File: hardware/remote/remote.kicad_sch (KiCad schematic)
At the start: 34 parts, among them J1 USB-C, Q1 MMBT3904, Q2 MMBT3904, SW1 UP, SW2 DOWN, SW3 ON/OFF, U1 TP4056, U2 ME6211C33M5G, U3 ESP32-WROOM-32, U4 CP2102

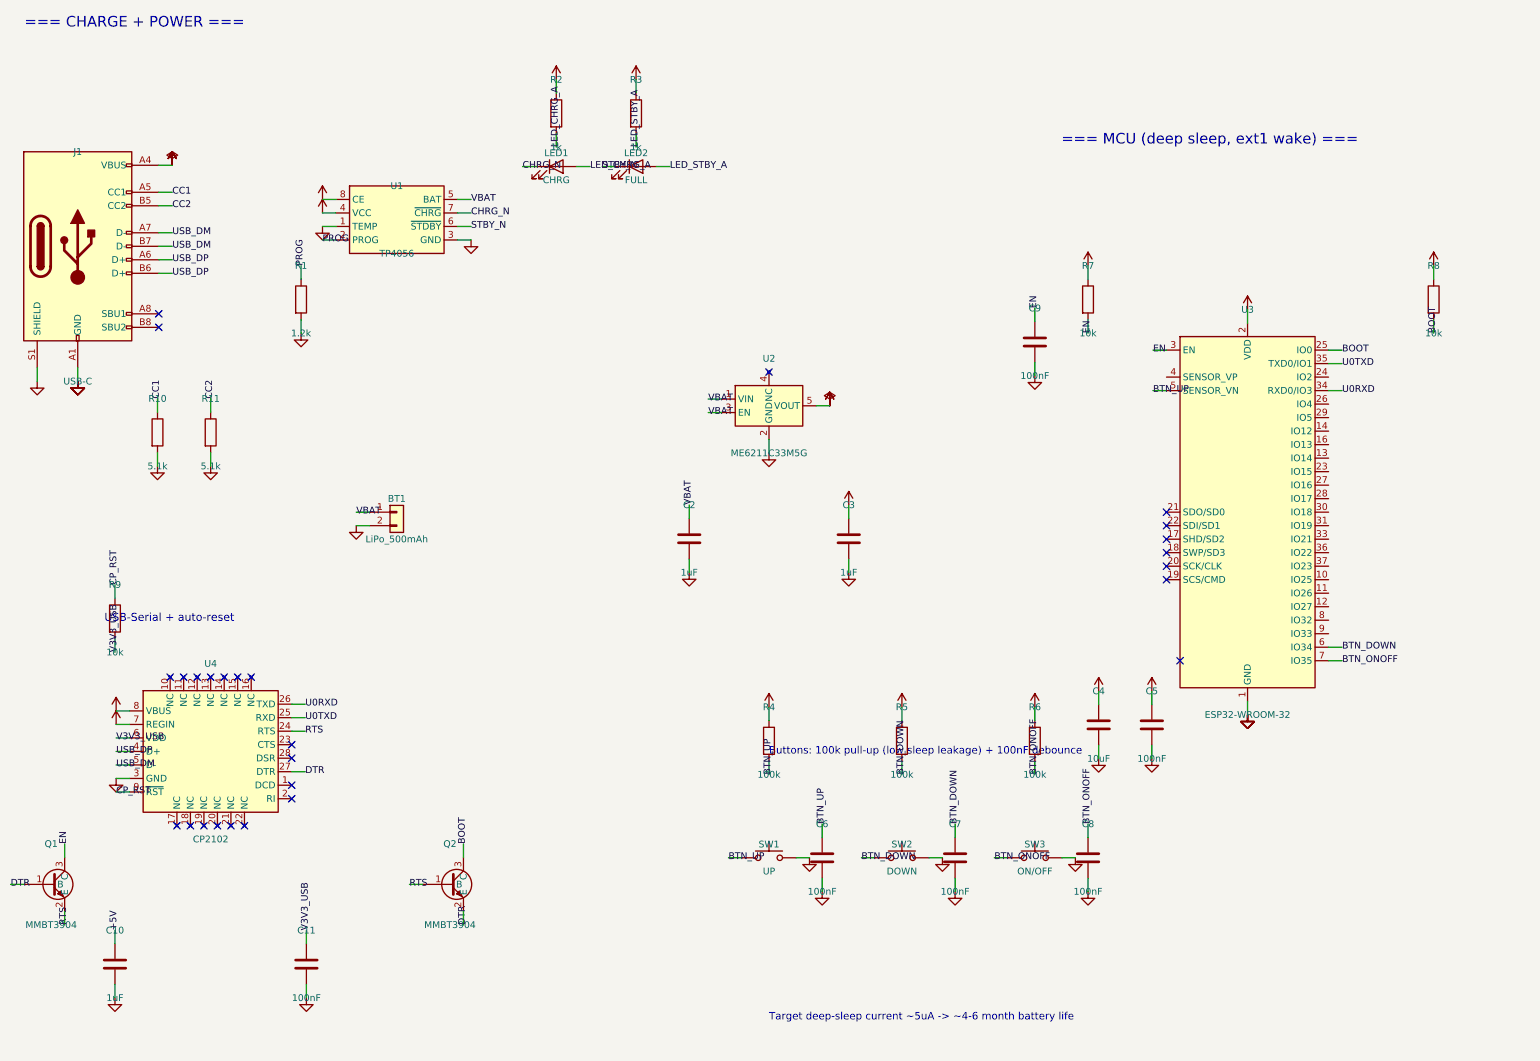
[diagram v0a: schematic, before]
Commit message: hardware: switch both boards to plug-in modules (ESP32 DevKit, TP4056)
Rework the schematic capture so every part maps to a hand-solderable module
or component you can buy from Robu / Robocraze / Quartz Components, per the
"hand-solder from modules" plan.

Both boards:
- Replace the bare ESP32-WROOM-32 + the entire onboard USB-serial subsystem
  (CP2102 QFN, board USB-C + CC resistors, two-transistor auto-reset, CP2102
  support caps/pull-ups, separate BOOT/EN buttons) with a plug-in ESP32
  DevKit V1 (30-pin) that carries its own USB bridge, micro-USB, auto-reset
  and BOOT/EN. Carrier now only routes 3V3/GND + the GPIOs it uses.

Remote:
- TP4056 bare SOP-8 -> TP4056 charge+protect module (charges via its own
  USB-C); external charge LEDs + PROG resistor removed (onboard the module).
  B+/B- -> LiPo, OUT+/OUT- -> ME6211 input.
- Tactile buttons -> 6mm THT footprint (SW_PUSH_6mm).
- Note: DevKit leaks in deep sleep, so battery life drops from months to
  days/weeks (accepted trade for simplicity; documented in CLAUDE.md).

parts.py: add ESP32_DevKit() and TP4056_module() symbols; drop bare CP2102 /
TP4056. Regenerated via gen_dimmer.py / gen_remote.py; validate.py reports no
floating pins on either board. Schematic files normalize back to the
generator's 20230121 format (KiCad 10 re-upgrades on open).
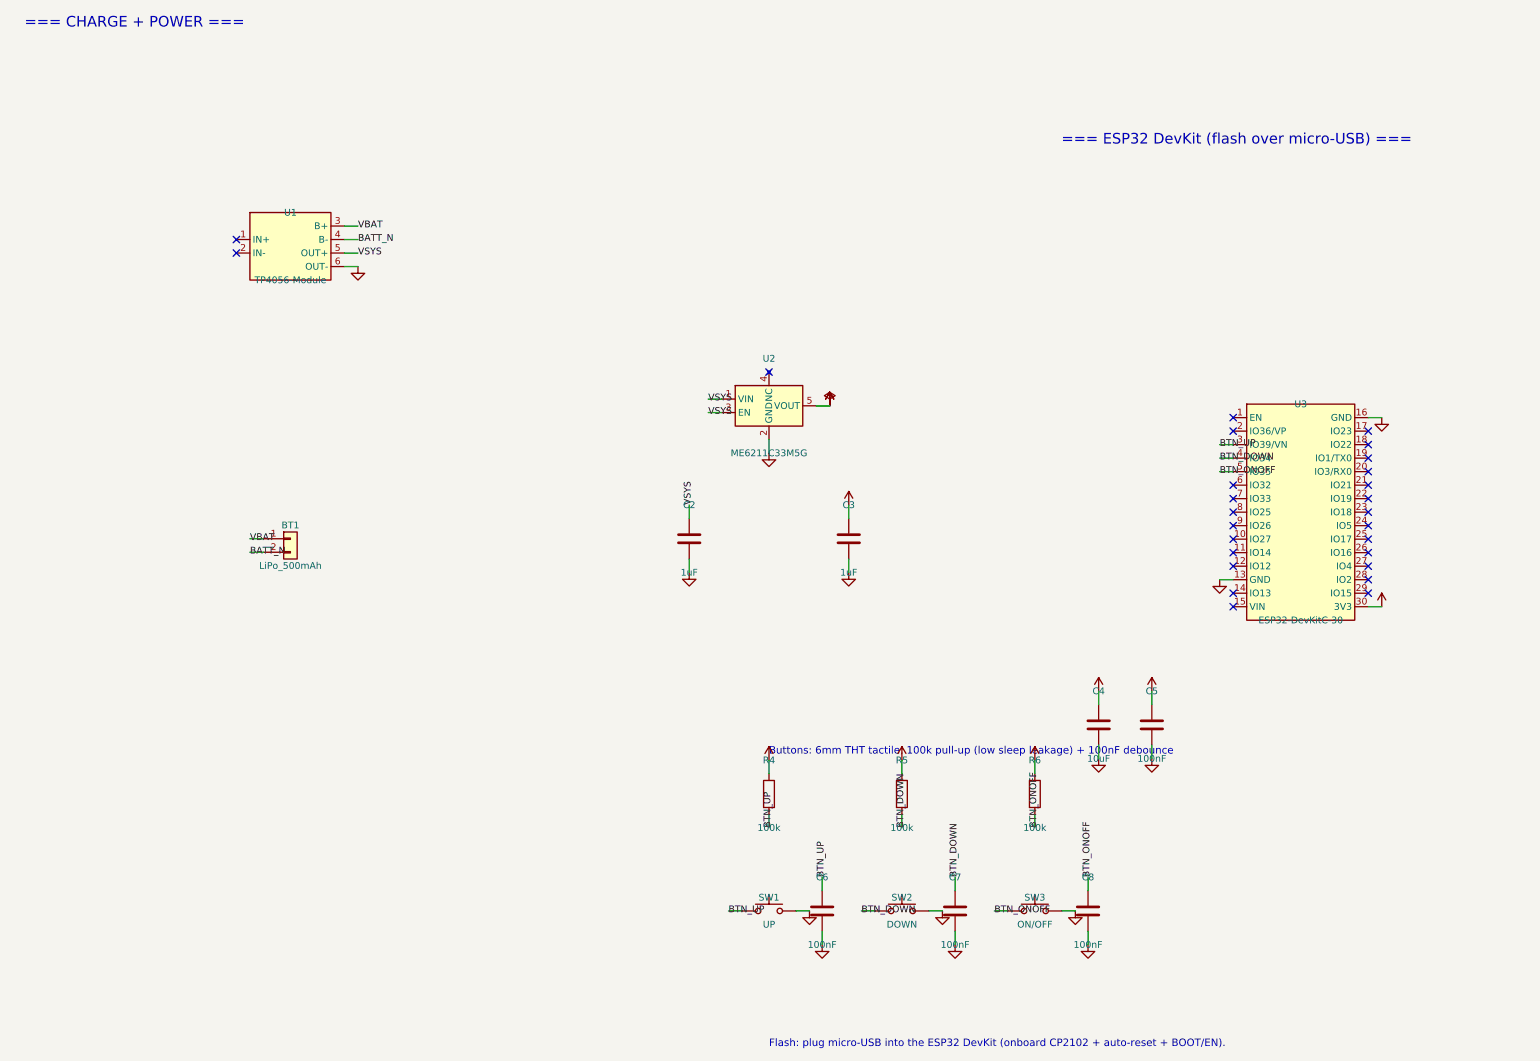
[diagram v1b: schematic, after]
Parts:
- removed C10: 1uF, Capacitor_SMD:C_0805_2012Metric, symbol Device:C
- removed C11, C9: 100nF, Capacitor_SMD:C_0805_2012Metric, symbol Device:C
- removed J1: USB-C, Connector_USB:USB_C_Receptacle_HRO_TYPE-C-31-M-12, symbol Connector:USB_C_Receptacle_USB2.0_16P
- removed LED1: CHRG, LED_SMD:LED_0805_2012Metric, symbol Device:LED
- removed LED2: FULL, LED_SMD:LED_0805_2012Metric, symbol Device:LED
- removed Q1, Q2: MMBT3904, Package_TO_SOT_SMD:SOT-23, symbol Transistor_BJT:MMBT3904
- removed R1: 1.2k, Resistor_SMD:R_0805_2012Metric, symbol Device:R
- removed R10, R11: 5.1k, Resistor_SMD:R_0805_2012Metric, symbol Device:R
- removed R2, R3: 1k, Resistor_SMD:R_0805_2012Metric, symbol Device:R
- removed R7, R8, R9: 10k, Resistor_SMD:R_0805_2012Metric, symbol Device:R
- removed U1: TP4056, Package_SO:SOIC-8_3.9x4.9mm_P1.27mm, symbol Battery_Management:TP4056
- removed U3: ESP32-WROOM-32, RF_Module:ESP32-WROOM-32, symbol RF_Module:ESP32-WROOM-32
- removed U4: CP2102, Package_DFN_QFN:QFN-28-1EP_5x5mm_P0.5mm, symbol Interface_USB:CP2102
- added U1: TP4056-Module, Connector_PinHeader_2.54mm:PinHeader_1x06_P2.54mm_Vertical, symbol Battery_Management:TP4056_Module
- added U3: ESP32-DevKitC-30, Module:ESP32-DevKitC, symbol Module:ESP32-DevKitC
- SW1, SW2, SW3: footprint Button_Switch_SMD:SW_SPST_PTS645 -> Button_Switch_THT:SW_PUSH_6mm
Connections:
- net +3V3: now also U3.30 (3V3)
- net BTN_DOWN: now also U3.4 (IO34)
- net BTN_ONOFF: now also U3.5 (IO35)
- net BTN_UP: now also U3.3 (IO39/VN)
- net GND: now also U1.6 (OUT-), U3.13 (GND), U3.16 (GND); no longer BT1.2 (Pin_2)
- net VBAT: now also U1.3 (B+); no longer C2.1, U2.1 (VIN), U2.3 (EN)
- new net BATT_N: BT1.2 (Pin_2), U1.4 (B-)
- new net VSYS: C2.1, U1.5 (OUT+), U2.1 (VIN), U2.3 (EN)
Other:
- note added: "=== ESP32 DevKit (flash over micro-USB) ==="
- note added: "Buttons: 6mm THT tactile, 100k pull-up (low sleep leakage) + 100nF debounce"
- note added: "Flash: plug micro-USB into the ESP32 DevKit (onboard CP2102 + auto-reset + BOOT/EN)."
- note removed: "=== MCU (deep sleep, ext1 wake) ==="
- note removed: "Buttons: 100k pull-up (low sleep leakage) + 100nF debounce"
- note removed: "Target deep-sleep current ~5uA -> ~4-6 month battery life"
- note removed: "USB-Serial + auto-reset"

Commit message: hardware: annotate both schematics with block boxes, headers, net legend
Add color-coded functional-block rectangles, colored block-title text,
and a signal/net-legend glossary to the dimmer and remote schematics for
readability. Also upgrades both .kicad_sch to KiCad 10 format. Netlist
connectivity verified unchanged on both boards (dimmer 12 nets, remote 8).
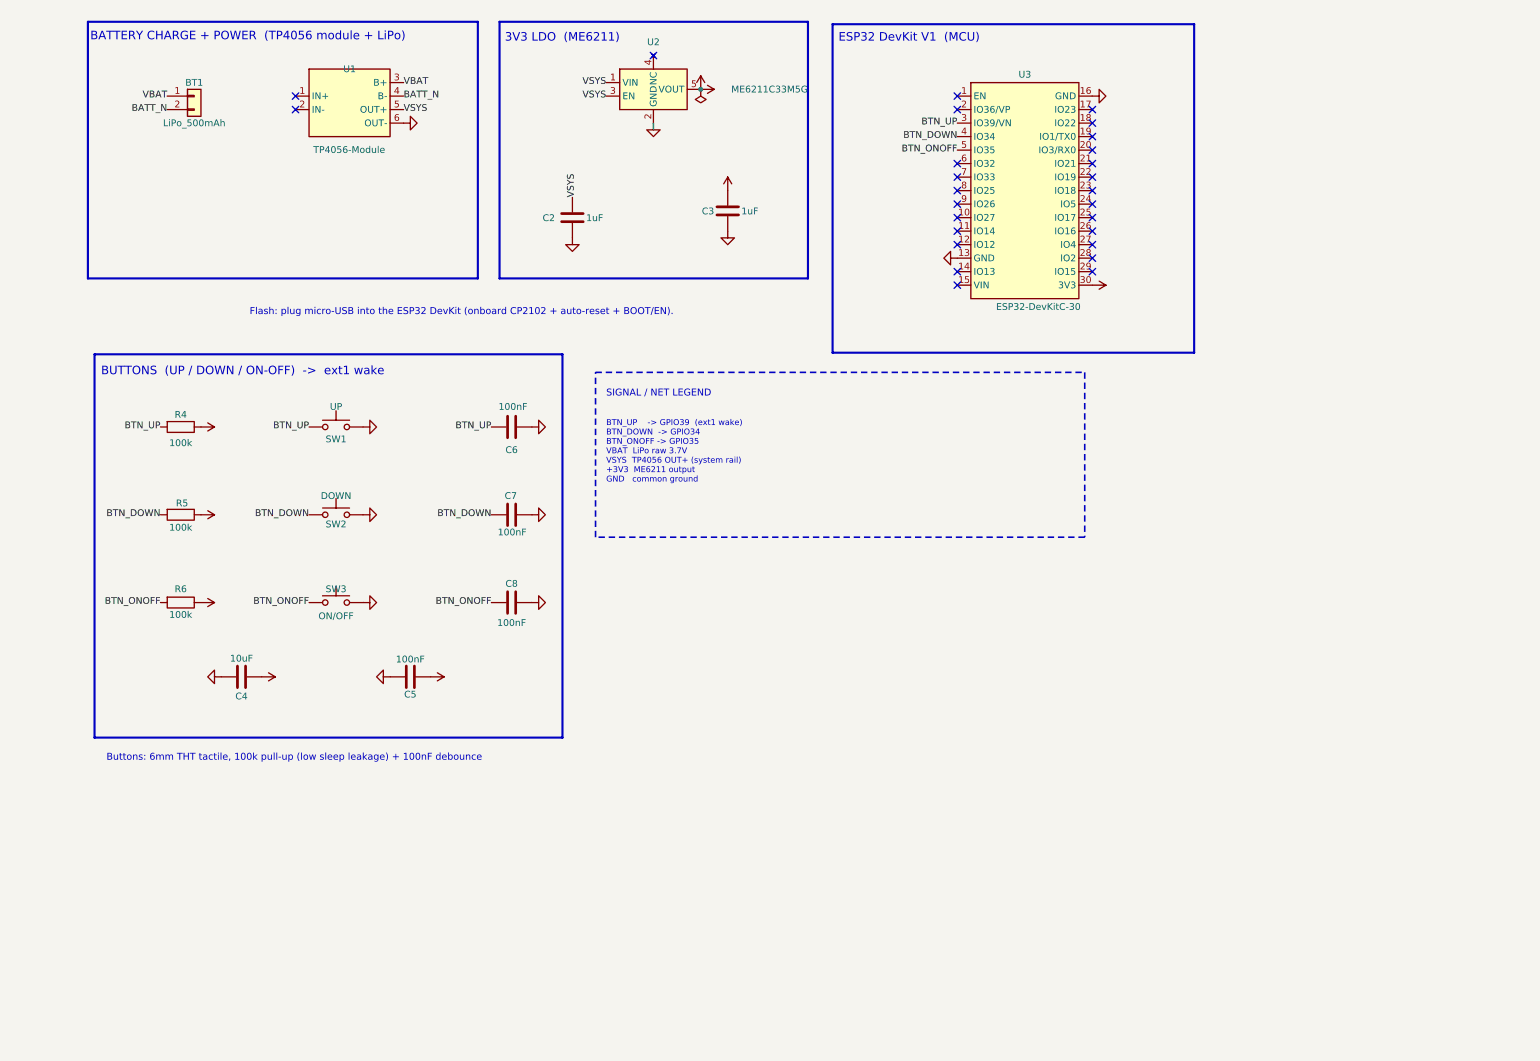
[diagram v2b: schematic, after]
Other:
- note added: "3V3 LDO (ME6211)"
- note added: "BATTERY CHARGE + POWER (TP4056 module + LiPo)"
- note added: "BTN_UP -> GPIO39 (ext1 wake) BTN_DOWN -> GPIO34 BTN_ONOFF -> GPIO35 VBAT LiPo raw 3.7V VSYS TP4056 OUT+ (system rail) +3V3 ME6211 output GND common ground"
- note added: "BUTTONS (UP / DOWN / ON-OFF) -> ext1 wake"
- note added: "ESP32 DevKit V1 (MCU)"
- note added: "SIGNAL / NET LEGEND"
- note removed: "=== CHARGE + POWER ==="
- note removed: "=== ESP32 DevKit (flash over micro-USB) ==="
- moved on the sheet: BT1, C2, C3, C4, C5, C6, C7, C8, R4, R5, R6, SW1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

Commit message: hardware(remote): first-pass PCB layout (placement + netlist + outline)
Bootstraps the remote board PCB from the captured schematic.

- gen_remote_pcb.py: kiutils-based PCB generator. Loads real KiCad footprints,
  places every part in functional groups (charge/power on the left, DevKit on
  the right, three button stacks along the bottom), assigns the full schematic
  netlist to the pads, and draws the Edge.Cuts outline (78x60mm). Includes a
  pad-bbox overlap self-check (no GUI DRC here). Traces + GND pour are the next
  pass. Netlist is taken from a freshly generated kiutils-native schematic, not
  the committed file, because KiCad re-saved the schematic into a newer format
  that kiutils under-parses.

- Custom footprint IoT_AC_Dimmer:ESP32-DevKitC-30 (30-pin DevKit V1, two 1x15
  rows at 0.9in). Registered via project fp-lib-tables. Schematic footprint
  field updated to reference it (was a non-existent placeholder).

- gen_remote.py: REMOTE_SCH_OUT env override so tooling can emit a scratch
  schematic without touching the committed one.

Verified: 17 footprints, 8 nets, 48 netted pads, no overlaps, in-outline.

NOTE (first pass to verify in KiCad): the DevKit footprint row spacing (0.9in)
and the TP4056-module pad mapping should be checked against the physical parts
before fab; routing and the GND pour are still to do.
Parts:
- U3: footprint Module:ESP32-DevKitC -> IoT_AC_Dimmer:ESP32-DevKitC-30; symbol Module:ESP32-DevKitC -> IoT_AC_Dimmer:ESP32-DevKitC-30
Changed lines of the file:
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@@
 	)
 	(symbol
-		(lib_id "Module:ESP32-DevKitC")
+		(lib_id "IoT_AC_Dimmer:ESP32-DevKitC-30")
 		(at 198.12 49.53 0)
 		(unit 1)
@@
 			)
 		)
-		(property "Footprint" "Module:ESP32-DevKitC"
+		(property "Footprint" "IoT_AC_Dimmer:ESP32-DevKitC-30"
 			(at 198.12 49.53 0)
 			(hide yes)

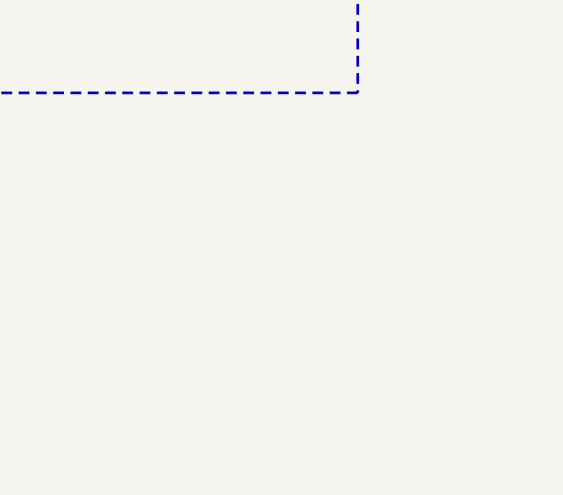
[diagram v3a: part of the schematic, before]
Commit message: pcb: Update PCB design and Child item name
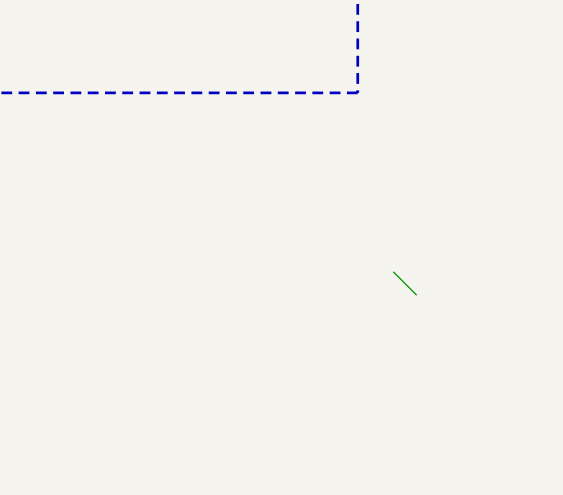
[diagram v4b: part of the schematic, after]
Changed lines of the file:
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@@
 		(at 210.82 46.99)
+	)
+	(bus_entry
+		(at 213.36 134.62)
+		(size 2.54 2.54)
+		(stroke
+			(width 0)
+			(type default)
+		)
 	)
 	(wire
